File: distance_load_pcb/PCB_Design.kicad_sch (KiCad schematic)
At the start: 15 parts, among them J1 From Power Source 5V, J2 From Limit Switch (LS), J3 From Encoder (EC), J4 Debug output, J5 Screen_Front, J6 Screen_Back, J7 From Load Cell (LC), U1 ESP-01v090, U3 YAAJ_BluePill_Part_Like

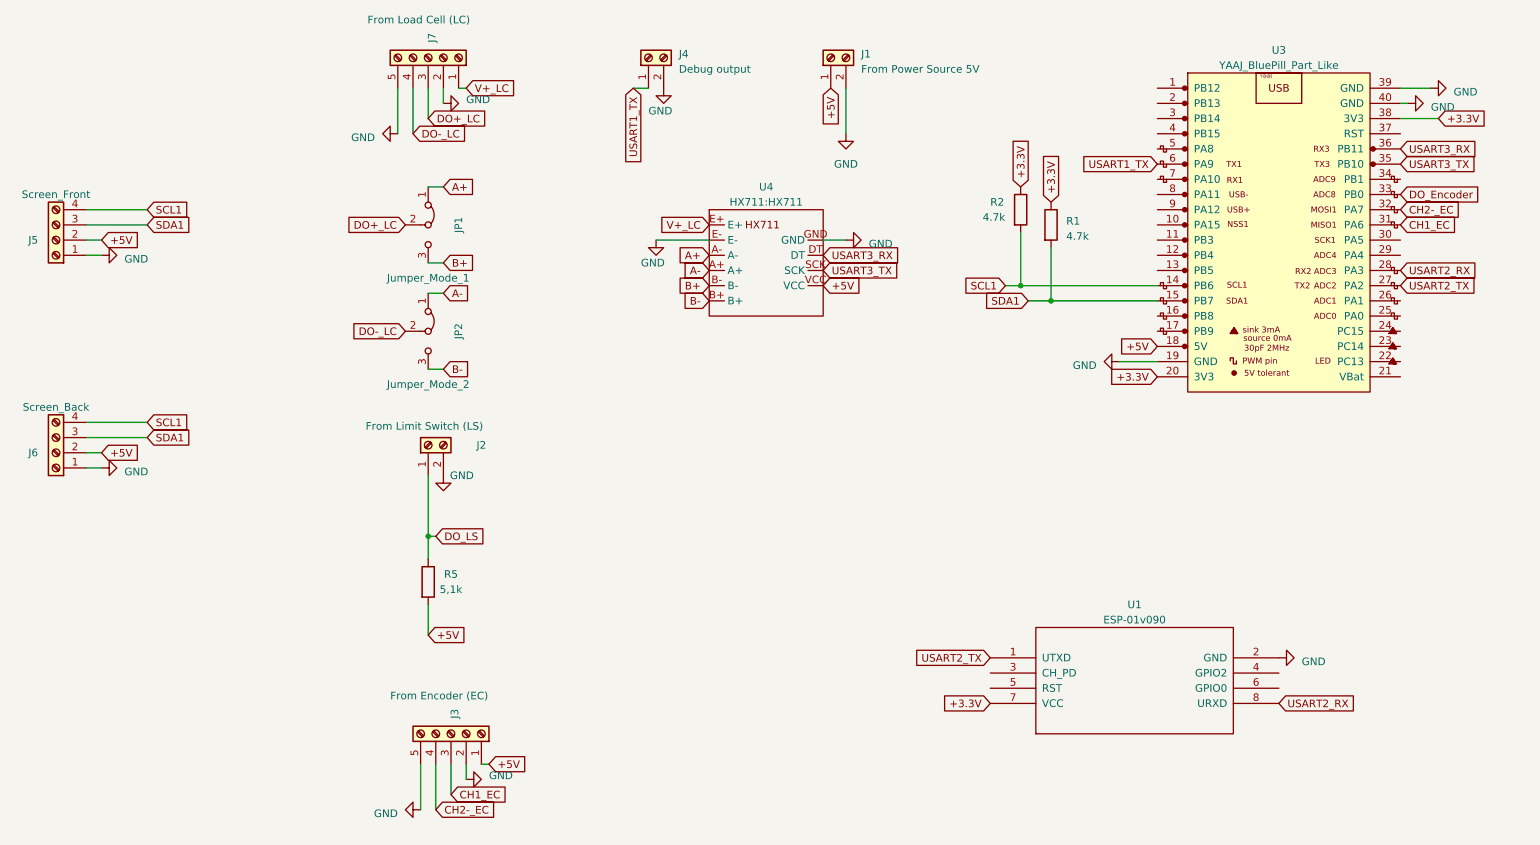
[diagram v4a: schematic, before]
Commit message: felipin's suggestions, all the tracs arrive at the components by the bottom
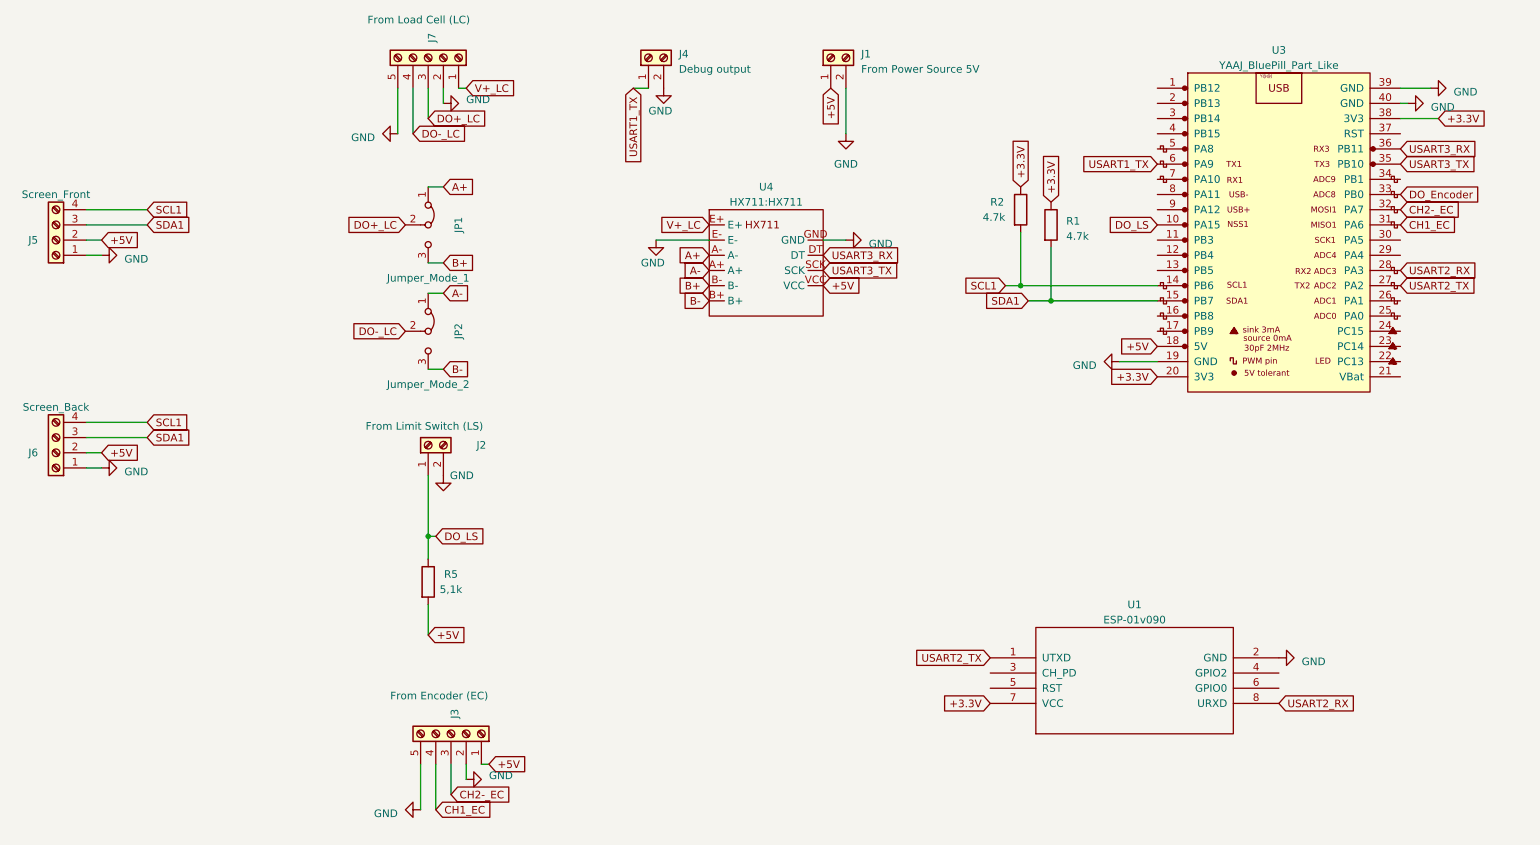
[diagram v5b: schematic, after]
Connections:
- net CH1_EC: now also J3.4 (Pin_4); no longer J3.3 (Pin_3)
- net CH2-_EC: now also J3.3 (Pin_3); no longer J3.4 (Pin_4)
- net DO_LS: now also U3.10 (PA15)
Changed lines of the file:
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@@
     (stroke (width 0) (type default))
   )
+  (global_label "DO_LS" (shape input) (at 218.44 52.07 180) (fields_autoplaced)
+    (effects (font (size 1.27 1.27)) (justify right))
+    (property "Intersheetrefs" "${INTERSHEET_REFS}" (at 209.7285 52.07 0)
+      (effects (font (size 1.27 1.27)) (justify right) hide)
+    )
+  )
   (global_label "DO_Encoder" (shape input) (at 259.08 46.99 0) (fields_autoplaced)
     (effects (font (size 1.27 1.27)) (justify left))
@@
     )
   )
-  (global_label "CH1_EC" (shape input) (at 100.33 147.32 0) (fields_autoplaced)
-    (effects (font (size 1.27 1.27)) (justify left))
-    (property "Intersheetrefs" "${INTERSHEET_REFS}" (at 110.4324 147.32 0)
+  (global_label "CH1_EC" (shape input) (at 97.79 149.86 0) (fields_autoplaced)
+    (effects (font (size 1.27 1.27)) (justify left))
+    (property "Intersheetrefs" "${INTERSHEET_REFS}" (at 107.8924 149.86 0)
       (effects (font (size 1.27 1.27)) (justify left) hide)
     )
@@
     )
   )
-  (global_label "CH2-_EC" (shape input) (at 97.79 149.86 0) (fields_autoplaced)
-    (effects (font (size 1.27 1.27)) (justify left))
-    (property "Intersheetrefs" "${INTERSHEET_REFS}" (at 109.4648 149.86 0)
-      (effects (font (size 1.27 1.27)) (justify left) hide)
-    )
+  (global_label "CH2-_EC" (shape input) (at 100.33 147.32 0) (fields_autoplaced)
+    (effects (font (size 1.27 1.27)) (justify left))
+    (property "Intersheetrefs" "${INTERSHEET_REFS}" (at 112.0048 147.32 0)
+      (effects (font (size 1.27 1.27)) (justify left) hide)
+    )

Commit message: fix pcb
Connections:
- net DO_Encoder is gone; now on net DO_LS: U3.33 (PB0)
- net DO_LS: no longer U3.10 (PA15)
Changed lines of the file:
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@@
     (stroke (width 0) (type default))
-  )
-  (global_label "DO_LS" (shape input) (at 218.44 52.07 180) (fields_autoplaced)
-    (effects (font (size 1.27 1.27)) (justify right))
-    (property "Intersheetrefs" "${INTERSHEET_REFS}" (at 209.7285 52.07 0)
-      (effects (font (size 1.27 1.27)) (justify right) hide)
-    )
-  )
-  (global_label "DO_Encoder" (shape input) (at 259.08 46.99 0) (fields_autoplaced)
-    (effects (font (size 1.27 1.27)) (justify left))
-    (property "Intersheetrefs" "${INTERSHEET_REFS}" (at 273.1133 46.99 0)
-      (effects (font (size 1.27 1.27)) (justify left) hide)
-    )
   )
   (global_label "USART3_TX" (shape input) (at 259.08 41.91 0) (fields_autoplaced)
@@
     )
   )
+  (global_label "DO_LS" (shape input) (at 259.08 46.99 0) (fields_autoplaced)
+    (effects (font (size 1.27 1.27)) (justify left))
+    (property "Intersheetrefs" "${INTERSHEET_REFS}" (at 267.7915 46.99 0)
+      (effects (font (size 1.27 1.27)) (justify left) hide)
+    )
+  )

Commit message: Vamos Solsticio!
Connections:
- net A+: now also JP2.1 (A), U4.A+; no longer JP1.1 (A), U4.A-
- net A-: now also JP1.1 (A), U4.A-; no longer JP2.1 (A), U4.A+
- net B+: now also JP2.3 (B), U4.B+; no longer JP1.3 (B), U4.B-
- net B-: now also JP1.3 (B), U4.B-; no longer JP2.3 (B), U4.B+
- net DO+_LC: now also J7.4 (Pin_4), JP2.2 (C); no longer J7.3 (Pin_3), JP1.2 (C)
- net DO-_LC: now also J7.3 (Pin_3), JP1.2 (C); no longer J7.4 (Pin_4), JP2.2 (C)
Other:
- moved on the sheet: JP1
